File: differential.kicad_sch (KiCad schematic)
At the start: 15 parts, among them J2 DIFF_1, U2 SN74LVC2G17DBVR

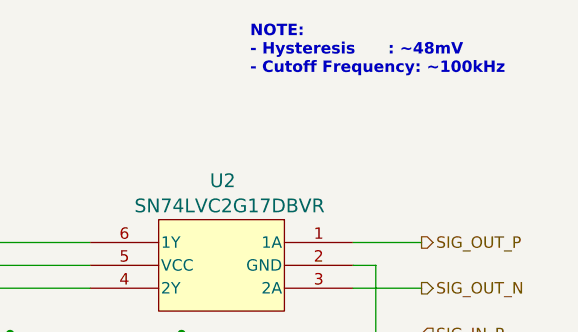
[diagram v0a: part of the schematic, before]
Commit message: New design; reduce MCU pin count; utilize new connectors
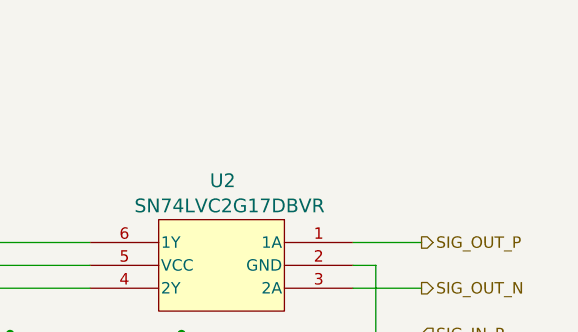
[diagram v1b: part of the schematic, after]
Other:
- note removed: "NOTE: - Hysteresis : ~48mV - Cutoff Frequency: ~100kHz"
